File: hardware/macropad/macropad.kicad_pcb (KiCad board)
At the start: 2 copper layers, 162.9 x 95.3 mm, 93 parts, among them J1 SWD, J10 Conn_01x02, J2 USB_C_Receptacle_USB2.0_16P, J3 Conn_01x02, J4 display(4x1), J5 Conn_01x04_Pin, J6 Conn_01x03_Socket, J8 Conn_01x02, J9 USB_A, Q1 Q_PMOS, Q2 FS8205A, SW1 SW_Push, SW10 SW_SPDT, SW12 RotaryEncoder_Switch, SW13 RotaryEncoder_Switch, SW2 SW_Push, SW3 SW_Push, SW4 SW_Push, SW5 SW_Push, SW6 SW_Push, SW7 SW_Push, SW8 SW_Push, SW9 SW_Push, U1 LP2992IM5-3.3/NOPB, U2 STM32F103C8Tx, U3 NRF24L01_Breakout, U4 STM32F103C8Tx, U5 NRF24L01_Breakout, U6 TP4056-42-ESOP8, U7 DW01A, U9 LP2992IM5-3.3/NOPB, Y1 8Mhz C_L=12pF, Y2 8Mhz

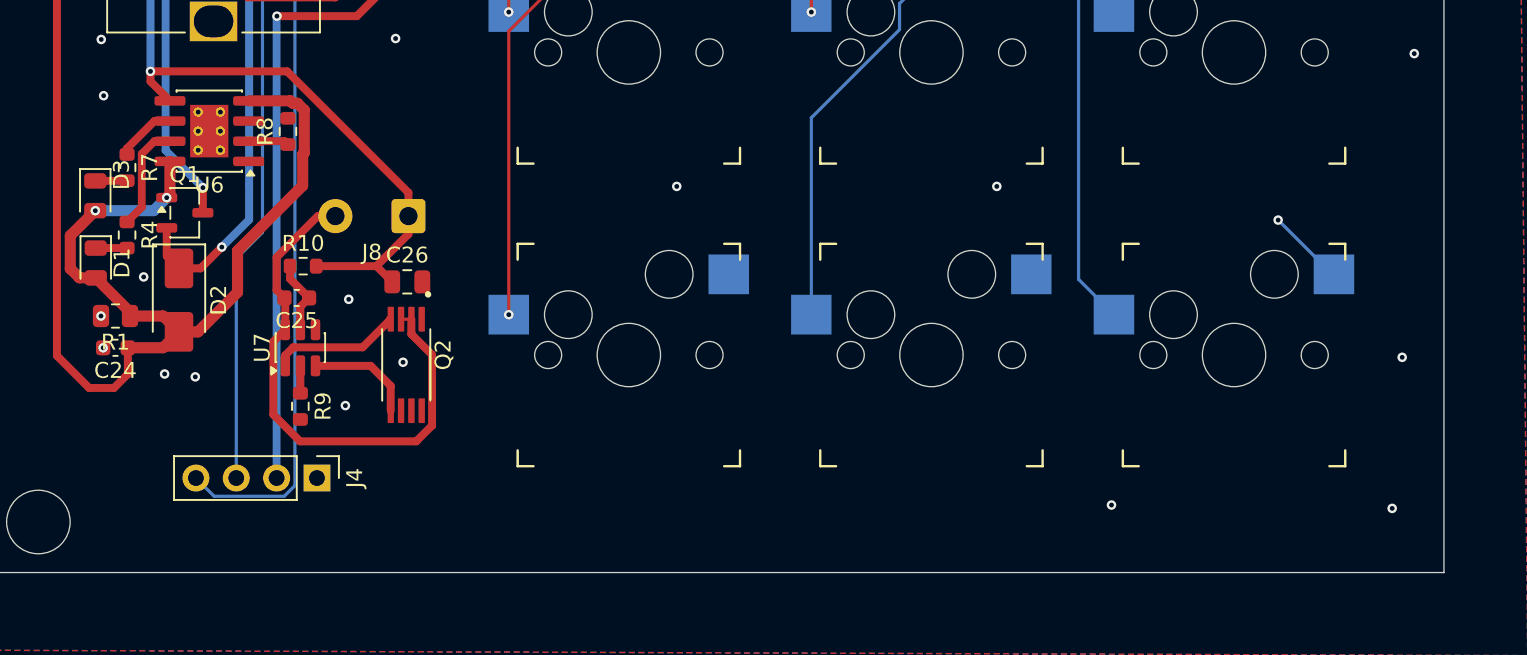
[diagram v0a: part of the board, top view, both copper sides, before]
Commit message: schottkey updated and added mount hole
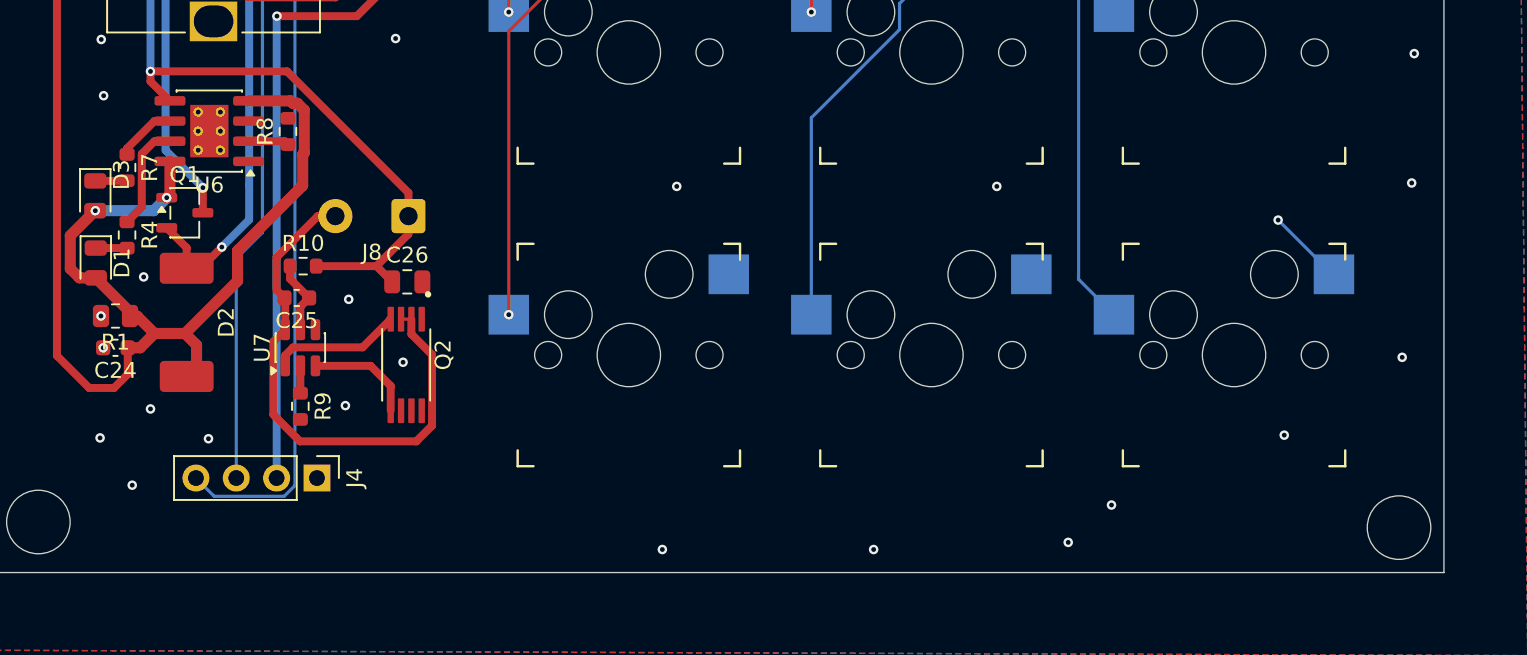
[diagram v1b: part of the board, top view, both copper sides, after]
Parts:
- moved D2 1.48 mm to (61.1, 121.5)
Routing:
- net VBUS: track 179.2 -> 180.5 mm
- net GND: vias 74 -> 80
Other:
- outline, holes or cut-outs redrawn

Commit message: stitching done
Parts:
- added REF**: MouseBite-Slot_2.0x2.0mm_inset_D0.5mm_P0.85mm_5h, Panelization:MouseBite-Slot_2.0x2.0mm_inset_D0.5mm_P0.85mm_5h, F.Cu at (140.6, 135.5)
- added REF**: MouseBite-Slot_2.0x2.0mm_inset_D0.5mm_P0.85mm_5h, Panelization:MouseBite-Slot_2.0x2.0mm_inset_D0.5mm_P0.85mm_5h, F.Cu at (142.6, 95.8)
- added REF**: MouseBite-Slot_2.0x2.0mm_inset_D0.5mm_P0.85mm_5h, Panelization:MouseBite-Slot_2.0x2.0mm_inset_D0.5mm_P0.85mm_5h, F.Cu at (142.6, 127.8)
- added REF**: MouseBite-Slot_2.0x2.0mm_inset_D0.5mm_P0.85mm_5h, Panelization:MouseBite-Slot_2.0x2.0mm_inset_D0.5mm_P0.85mm_5h, F.Cu at (142.6, 111.8)
- added REF**: MouseBite-Slot_2.0x2.0mm_inset_D0.5mm_P0.85mm_5h, Panelization:MouseBite-Slot_2.0x2.0mm_inset_D0.5mm_P0.85mm_5h, F.Cu at (142.6, 103.8)
- added REF**: MouseBite-Slot_2.0x2.0mm_inset_D0.5mm_P0.85mm_5h, Panelization:MouseBite-Slot_2.0x2.0mm_inset_D0.5mm_P0.85mm_5h, F.Cu at (142.6, 119.8)
- moved C21 72.7 mm to (151.0, 132.0), turned to 180 degrees
- moved C16 70.3 mm to (151.0, 130.1), turned to 180 degrees
- moved U1 66.2 mm to (154.8, 131.1), turned to 180 degrees
- moved C10 62.3 mm to (147.6, 116.7), turned to 180 degrees
- moved C13 61.9 mm to (158.1, 131.1), turned to -90 degrees
- moved Y2 60.7 mm to (147.6, 113.7), turned to 90 degrees
- moved C15 59.5 mm to (147.6, 110.7), turned to 0 degrees
- moved C20 54.4 mm to (150.1, 109.9), turned to 90 degrees
- moved R22 54.3 mm to (151.0, 114.2), turned to 180 degrees
- moved R5 54.3 mm to (150.0, 106.3), turned to 90 degrees
- moved C11 53.5 mm to (152.0, 115.9), turned to 180 degrees
- moved C23 50.8 mm to (158.4, 123.8), turned to 180 degrees
- moved C19 50.4 mm to (152.3, 102.6), turned to 180 degrees
- moved J5 49.1 mm to (162.5, 126.4), turned to 0 degrees
- moved J9 48.4 mm to (155.0, 96.8), turned to 180 degrees
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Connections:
- C10 pad 2: GND_DGL -> GND
- C11 pad 2: GND_DGL -> GND
- C12 pad 2: GND_DGL -> GND
- C13 pad 2: GND_DGL -> GND
- C14 pad 2: GND_DGL -> GND
- C15 pad 2: GND_DGL -> GND
- C16 pad 2: GND_DGL -> GND
- C19 pad 2: GND_DGL -> GND
- C20 pad 2: GND_DGL -> GND
- C21 pad 2: GND_DGL -> GND
- C22 pad 1: GND_DGL -> GND
- C23 pad 2: GND_DGL -> GND
- C7 pad 2: GND_DGL -> GND
- J10 pad 2: GND_DGL -> GND
- J5 pad 4: GND_DGL -> GND
- J9 pad 4: GND_DGL -> GND
- J9 pad 5: GND_DGL -> GND
- R3 pad 2: GND_DGL -> GND
- R5 pad 2: GND_DGL -> GND
- U1 pad 2: GND_DGL -> GND
- U4 pad 23: GND_DGL -> GND
- U4 pad 35: GND_DGL -> GND
- U4 pad 47: GND_DGL -> GND
- U4 pad 8: GND_DGL -> GND
- U5 pad 1: GND_DGL -> GND
- Y2 pad 2: GND_DGL -> GND
- Y2 pad 4: GND_DGL -> GND
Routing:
- net GND_DGL: track 22.1 -> 0.00 mm, vias 38 -> 0
- net VBUS: track 180.5 -> 161.8 mm
- net GND: track 27.7 -> 20.3 mm, vias 80 -> 197
- net /dongle/HSE_IN_DGL: track 12.8 -> 11.0 mm
- net /SWDIO: track 25.7 -> 27.4 mm, vias 3 -> 2
- net VBUS_DGL: track 59.4 -> 60.8 mm
- net /Power/Vout_buck: track 26.1 -> 24.7 mm
- net /dongle/HSE_OUT_DGL: track 15.3 -> 14.3 mm
- net /PA5: track 11.8 -> 11.0 mm
- net Net-(J2-CC1): track 15.3 -> 14.7 mm
- net /Power/B-: track 34.2 -> 33.6 mm
- net /SWCLK: track 30.5 -> 31.1 mm
- net /SDAPB7: track 98.7 -> 98.1 mm
- net /K4: vias 2 -> 1
- net +3.3V: vias 3 -> 2
- removed copper zone on B.Cu, net GND_DGL
- removed copper zone on F.Cu, net GND_DGL
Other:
- board size 162.9 x 95.3 mm -> 116.2 x 95.4 mm

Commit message: fab outputs
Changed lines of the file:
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@@
 			(outputformat 1)
 			(mirror no)
-			(drillshape 1)
+			(drillshape 0)
 			(scaleselection 1)
-			(outputdirectory "")
+			(outputdirectory "./")
 		)
 	)
@@
 		(tags "connector Hirose DF13 vertical")
 		(property "Reference" "J10"
-			(at 0.395 -1.562024 -90)
+			(at 0.395 -1.562024 270)
 			(layer "F.SilkS")
 			(effects
@@
 	)
 	(gr_line
-		(start 166.55 137.49)
-		(end 166.55 93.75)
+		(start 166.54 93.75)
+		(end 166.55 137.49)
 		(stroke
 			(width 0.05)

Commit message: proper fab outs
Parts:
- C24, C25: value 0.1u -> 100n
- R6: value 1.5K -> 1.5k
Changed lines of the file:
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@@
 		(sheetname "/Power/")
 		(sheetfile "macropad_power.kicad_sch")
-		(attr through_hole)
+		(attr through_hole dnp)
 		(pad "1" thru_hole roundrect
 			(at 0 0 180)
@@
 		(sheetname "/")
 		(sheetfile "macropad.kicad_sch")
-		(attr smd)
+		(attr smd dnp)
 		(fp_line
 			(start -7 -6)
@@
 		(sheetname "/")
 		(sheetfile "macropad.kicad_sch")
-		(attr smd)
+		(attr smd dnp)
 		(fp_line
 			(start -7 -6)
@@
 		(sheetname "/")
 		(sheetfile "macropad.kicad_sch")
-		(attr smd)
+		(attr smd dnp)
 		(fp_line
 			(start -7 -6)
@@
 		(sheetname "/")
 		(sheetfile "macropad.kicad_sch")
-		(attr smd)
+		(attr smd dnp)
 		(fp_line
 			(start -7 -6)
@@
 		(sheetname "/dongle/")
 		(sheetfile "dongle.kicad_sch")
-		(attr smd)
+		(attr smd dnp)
 		(fp_rect
 			(start -5.8 3.125)
@@
 		(sheetname "/")
 		(sheetfile "macropad.kicad_sch")
-		(attr through_hole)
+		(attr through_hole dnp)
 		(fp_line
 			(start -0.3 -1.6)
@@
 		(sheetname "/")
 		(sheetfile "macropad.kicad_sch")
-		(attr smd)
+		(attr smd dnp)
 		(fp_line
 			(start -7 -6)
@@
 		(sheetname "/Power/")
 		(sheetfile "macropad_power.kicad_sch")
-		(attr smd)
+		(attr smd dnp)
 		(fp_rect
 			(start -2 -11.5)
@@
 		(sheetname "/Power/")
 		(sheetfile "macropad_power.kicad_sch")
-		(attr exclude_from_pos_files)
+		(attr exclude_from_pos_files dnp)
 		(fp_rect
 			(start 2.8 -1.58)
@@
 		(sheetname "/")
 		(sheetfile "macropad.kicad_sch")
-		(attr through_hole)
+		(attr through_hole dnp)
 		(pad "1" thru_hole roundrect
 			(at 0 0 270)
@@
 		(sheetname "/")
 		(sheetfile "macropad.kicad_sch")
-		(attr through_hole)
+		(attr through_hole dnp)
 		(fp_line
 			(start -0.3 -1.6)
@@
 		(sheetname "/")
 		(sheetfile "macropad.kicad_sch")
-		(attr smd)
+		(attr smd dnp)
 		(fp_line
 			(start -7 -6)
@@
 			)
 		)
-		(property "Value" "0.1u"
+		(property "Value" "100n"
 			(at 0 1.43 0)
 			(layer "F.Fab")
@@
 		(sheetname "/")
 		(sheetfile "macropad.kicad_sch")
-		(attr smd)
+		(attr smd dnp)
 		(fp_line
 			(start -7 -6)
@@
 		(sheetname "/")
 		(sheetfile "macropad.kicad_sch")
-		(attr smd)
+		(attr smd dnp)
 		(fp_line
 			(start -7 -6)
@@
 		(sheetname "/")
 		(sheetfile "macropad.kicad_sch")
-		(attr through_hole)
+		(attr through_hole dnp)
 		(fp_line
 			(start -1.38 -1.38)
@@
 			)
 		)
-		(property "Value" "0.1u"
+		(property "Value" "100n"
 			(at 0 1.43 0)
 			(layer "F.Fab")
@@
 		(sheetname "/")
 		(sheetfile "macropad.kicad_sch")
-		(attr through_hole)
+		(attr through_hole dnp)
 		(fp_line
 			(start -1.38 9)
@@
 		(sheetname "/dongle/")
 		(sheetfile "dongle.kicad_sch")
-		(attr through_hole)
+		(attr through_hole dnp)
 		(fp_line
 			(start -1.27 -1.27)
@@
 			)
 		)
-		(property "Value" "1.5K"
+		(property "Value" "1.5k"
 			(at 0 1.43 0)
 			(layer "F.Fab")
@@
 		(sheetname "/")
 		(sheetfile "macropad.kicad_sch")
-		(attr smd)
+		(attr smd dnp)
 		(fp_line
 			(start -7 -6)
@@
 		(sheetname "/dongle/")
 		(sheetfile "dongle.kicad_sch")
-		(attr through_hole)
+		(attr through_hole dnp)
 		(fp_text user "${REFERENCE}"
 			(at 0.62 1.5 90)

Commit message: fixed technical queries
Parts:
- C10, C15, C17, C18: footprint Capacitor_SMD:C_0603_1608Metric -> Capacitor_SMD:C_0201_0603Metric
- R10: footprint Resistor_SMD:R_0603_1608Metric -> Resistor_SMD:R_0201_0603Metric
- U10: value ~ -> RT8010
- moved C18 1.72 mm to (98.9, 74.8), turned to 0 degrees
- moved C10 0.45 mm to (148.1, 116.6)
- moved C15 0.44 mm to (147.2, 110.8)
- moved C17 0.42 mm to (93.5, 71.9)
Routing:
- net GND: vias 197 -> 196
